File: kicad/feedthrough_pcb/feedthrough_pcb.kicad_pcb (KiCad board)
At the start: 2 copper layers, 150 x 150 mm, 2 parts, among them U1 LSHM-110-02.5-L-DV-A-S-TR, U2 LSHM-110-02.5-L-DV-A-S-TR

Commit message: updated feedthrough pcb
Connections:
- U2 pad 1: Net-(U1-Pad1) -> Net-(U2-Pad1)
- U2 pad 11: Net-(U1-Pad11) -> Net-(U2-Pad11)
- U2 pad 13: Net-(U1-Pad13) -> Net-(U2-Pad13)
- U2 pad 15: Net-(U1-Pad15) -> Net-(U2-Pad15)
- U2 pad 17: Net-(U1-Pad17) -> Net-(U2-Pad17)
- U2 pad 19: Net-(U1-Pad19) -> Net-(U2-Pad19)
- U2 pad 3: Net-(U1-Pad3) -> Net-(U2-Pad3)
- U2 pad 5: Net-(U1-Pad5) -> Net-(U2-Pad5)
- U2 pad 7: Net-(U1-Pad7) -> Net-(U2-Pad7)
- U2 pad 9: Net-(U1-Pad9) -> Net-(U2-Pad9)
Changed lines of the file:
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@@
     (zones 0)
     (modules 2)
-    (nets 21)
+    (nets 31)
   )
   (page A4)
@@
   )
   (setup
-    (last_trace_width 0.1524)
+    (last_trace_width 0.25)
     (user_trace_width 0.1524)
     (trace_clearance 0.2)
@@
     (solder_mask_min_width 0.25)
     (aux_axis_origin 0 0)
-    (visible_elements FFFFFF7F)
+    (visible_elements 7FFFFFFF)
     (pcbplotparams
       (layerselection 0x010fc_ffffffff)
@@
   (net 19 "Net-(U1-Pad19)")
   (net 20 "Net-(U1-Pad20)")
+  (net 21 "Net-(U2-Pad19)")
+  (net 22 "Net-(U2-Pad17)")
+  (net 23 "Net-(U2-Pad15)")
+  (net 24 "Net-(U2-Pad13)")
+  (net 25 "Net-(U2-Pad11)")
+  (net 26 "Net-(U2-Pad9)")
+  (net 27 "Net-(U2-Pad7)")
+  (net 28 "Net-(U2-Pad5)")
+  (net 29 "Net-(U2-Pad3)")
+  (net 30 "Net-(U2-Pad1)")
   (net_class Default "This is the default net class."
     (clearance 0.2)
@@
     (add_net "Net-(U1-Pad8)")
     (add_net "Net-(U1-Pad9)")
+    (add_net "Net-(U2-Pad1)")
+    (add_net "Net-(U2-Pad11)")
+    (add_net "Net-(U2-Pad13)")
+    (add_net "Net-(U2-Pad15)")
+    (add_net "Net-(U2-Pad17)")
+    (add_net "Net-(U2-Pad19)")
+    (add_net "Net-(U2-Pad3)")
+    (add_net "Net-(U2-Pad5)")
+    (add_net "Net-(U2-Pad7)")
+    (add_net "Net-(U2-Pad9)")
   )
   (module feedthrough_pcb:LSHM-110-02.5-L-DV-A-S-TR (layer B.Cu)
@@
       (effects (font (size 1 1) (thickness 0.15)) (justify mirror))
     )
-    (fp_text value LSHM-110-02.5-L-DV-A-S-TR (at 0 3.81) (layer B.Fab) hide
+    (fp_text value LSHM-110-02.5-L-DV-A-S-TR (at 0.1 -5.2) (layer B.Fab) hide
       (effects (font (size 1 1) (thickness 0.15)) (justify mirror))
     )
@@
       (effects (font (size 1 1) (thickness 0.15)))
     )
-    (fp_text value LSHM-110-02.5-L-DV-A-S-TR (at 0 -3.81) (layer F.Fab) hide
+    (fp_text value LSHM-110-02.5-L-DV-A-S-TR (at 0 5.5) (layer F.Fab) hide
       (effects (font (size 1 1) (thickness 0.15)))
     )
@@
       (net 20 "Net-(U1-Pad20)"))
     (pad 19 smd rect (at -2.29 1.75) (size 0.3 1.5) (layers F.Cu F.Paste F.Mask)
-      (net 19 "Net-(U1-Pad19)"))
+      (net 21 "Net-(U2-Pad19)"))
     (pad 18 smd rect (at -1.79 -1.75) (size 0.3 1.5) (layers F.Cu F.Paste F.Mask)
       (net 18 "Net-(U1-Pad18)"))
     (pad 17 smd rect (at -1.79 1.75) (size 0.3 1.5) (layers F.Cu F.Paste F.Mask)
-      (net 17 "Net-(U1-Pad17)"))
+      (net 22 "Net-(U2-Pad17)"))
     (pad 16 smd rect (at -1.29 -1.75) (size 0.3 1.5) (layers F.Cu F.Paste F.Mask)
       (net 16 "Net-(U1-Pad16)"))
     (pad 15 smd rect (at -1.29 1.75) (size 0.3 1.5) (layers F.Cu F.Paste F.Mask)
-      (net 15 "Net-(U1-Pad15)"))
+      (net 23 "Net-(U2-Pad15)"))
     (pad 14 smd rect (at -0.79 -1.75) (size 0.3 1.5) (layers F.Cu F.Paste F.Mask)
       (net 14 "Net-(U1-Pad14)"))
     (pad 13 smd rect (at -0.79 1.75) (size 0.3 1.5) (layers F.Cu F.Paste F.Mask)
-      (net 13 "Net-(U1-Pad13)"))
+      (net 24 "Net-(U2-Pad13)"))
     (pad 12 smd rect (at -0.29 -1.75) (size 0.3 1.5) (layers F.Cu F.Paste F.Mask)
       (net 12 "Net-(U1-Pad12)"))
     (pad 11 smd rect (at -0.29 1.75) (size 0.3 1.5) (layers F.Cu F.Paste F.Mask)
-      (net 11 "Net-(U1-Pad11)"))
+      (net 25 "Net-(U2-Pad11)"))
     (pad 10 smd rect (at 0.21 -1.75) (size 0.3 1.5) (layers F.Cu F.Paste F.Mask)
       (net 10 "Net-(U1-Pad10)"))
     (pad 9 smd rect (at 0.21 1.75) (size 0.3 1.5) (layers F.Cu F.Paste F.Mask)
-      (net 9 "Net-(U1-Pad9)"))
+      (net 26 "Net-(U2-Pad9)"))
     (pad 8 smd rect (at 0.71 -1.75) (size 0.3 1.5) (layers F.Cu F.Paste F.Mask)
       (net 8 "Net-(U1-Pad8)"))
     (pad 7 smd rect (at 0.71 1.75) (size 0.3 1.5) (layers F.Cu F.Paste F.Mask)
-      (net 7 "Net-(U1-Pad7)"))
+      (net 27 "Net-(U2-Pad7)"))
     (pad 6 smd rect (at 1.21 -1.75) (size 0.3 1.5) (layers F.Cu F.Paste F.Mask)
       (net 6 "Net-(U1-Pad6)"))
     (pad 5 smd rect (at 1.21 1.75) (size 0.3 1.5) (layers F.Cu F.Paste F.Mask)
-      (net 5 "Net-(U1-Pad5)"))
+      (net 28 "Net-(U2-Pad5)"))
     (pad 4 smd rect (at 1.71 -1.75) (size 0.3 1.5) (layers F.Cu F.Paste F.Mask)
       (net 4 "Net-(U1-Pad4)"))
     (pad 3 smd rect (at 1.71 1.75) (size 0.3 1.5) (layers F.Cu F.Paste F.Mask)
-      (net 3 "Net-(U1-Pad3)"))
+      (net 29 "Net-(U2-Pad3)"))
     (pad 2 smd rect (at 2.21 -1.75) (size 0.3 1.5) (layers F.Cu F.Paste F.Mask)
       (net 2 "Net-(U1-Pad2)"))
     (pad 1 smd rect (at 2.21 1.75) (size 0.3 1.5) (layers F.Cu F.Paste F.Mask)
-      (net 1 "Net-(U1-Pad1)"))
+      (net 30 "Net-(U2-Pad1)"))
   )
   (gr_circle (center 99.96 97.25) (end 174.96 97.25) (layer Edge.Cuts) (width 0.05))
-  (via (at 97.71 95) (size 0.5048) (drill 0.3) (layers F.Cu B.Cu) (net 20))
-  (via (at 98.21 99.5) (size 0.5048) (drill 0.3) (layers F.Cu B.Cu) (net 18))
-  (via (at 99.21 99.5) (size 0.5048) (drill 0.3) (layers F.Cu B.Cu) (net 14))
-  (via (at 100.21 99.5) (size 0.5048) (drill 0.3) (layers F.Cu B.Cu) (net 10))
-  (via (at 101.21 99.5) (size 0.5048) (drill 0.3) (layers F.Cu B.Cu) (net 6))
   (via (at 102.21 99.5) (size 0.5048) (drill 0.3) (layers F.Cu B.Cu) (net 2))
   (segment (start 102.21 98.25) (end 102.21 99.5) (width 0.1524) (layer F.Cu) (net 2))
@@
   (segment (start 101.71 97.51) (end 101.71 95) (width 0.1524) (layer F.Cu) (net 4))
   (segment (start 101.71 98.25) (end 101.71 97.51) (width 0.1524) (layer F.Cu) (net 4))
+  (via (at 101.21 99.5) (size 0.5048) (drill 0.3) (layers F.Cu B.Cu) (net 6))
   (segment (start 101.21 98.25) (end 101.21 99.5) (width 0.1524) (layer F.Cu) (net 6))
   (segment (start 101.21 96.99) (end 101.21 99.5) (width 0.1524) (layer B.Cu) (net 6))
@@
   (via (at 100.71 95) (size 0.5048) (drill 0.3) (layers F.Cu B.Cu) (net 8))
   (segment (start 100.71 98.25) (end 100.71 95) (width 0.1524) (layer F.Cu) (net 8))
+  (via (at 100.21 99.5) (size 0.5048) (drill 0.3) (layers F.Cu B.Cu) (net 10))
   (segment (start 100.21 98.25) (end 100.21 99.5) (width 0.1524) (layer F.Cu) (net 10))
   (segment (start 100.21 96.25) (end 100.21 99.5) (width 0.1524) (layer B.Cu) (net 10))
@@
   (via (at 99.71 95) (size 0.5048) (drill 0.3) (layers F.Cu B.Cu) (net 12))
   (segment (start 99.71 98.25) (end 99.71 95) (width 0.1524) (layer F.Cu) (net 12))
+  (via (at 99.21 99.5) (size 0.5048) (drill 0.3) (layers F.Cu B.Cu) (net 14))
   (segment (start 99.21 98.25) (end 99.21 99.5) (width 0.1524) (layer F.Cu) (net 14))
   (segment (start 99.21 96.25) (end 99.21 99.5) (width 0.1524) (layer B.Cu) (net 14))
@@
   (via (at 98.71 95) (size 0.5048) (drill 0.3) (layers F.Cu B.Cu) (net 16))
   (segment (start 98.71 98.25) (end 98.71 95) (width 0.1524) (layer F.Cu) (net 16))
+  (via (at 98.21 99.5) (size 0.5048) (drill 0.3) (layers F.Cu B.Cu) (net 18))
   (segment (start 98.21 98.25) (end 98.21 99.5) (width 0.1524) (layer F.Cu) (net 18))
   (segment (start 98.21 96.25) (end 98.21 99.5) (width 0.1524) (layer B.Cu) (net 18))
+  (via (at 97.71 95) (size 0.5048) (drill 0.3) (layers F.Cu B.Cu) (net 20))
   (segment (start 97.71 96.25) (end 97.71 95) (width 0.1524) (layer B.Cu) (net 20))
   (segment (start 97.71 97.3476) (end 97.71 95) (width 0.1524) (layer F.Cu) (net 20))

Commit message: updated feedthrough pcb
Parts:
- added U3: LSHM-110-02.5-L-DV-A-S-TR, feedthrough_pcb:LSHM-110-02.5-L-DV-A-S-TR, B.Cu at (87.7, 93.0)
- added U4: LSHM-110-02.5-L-DV-A-S-TR, feedthrough_pcb:LSHM-110-02.5-L-DV-A-S-TR, F.Cu at (87.7, 101.5)
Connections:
- U1 pad 1: Net-(U1-Pad1) -> GND
- U1 pad 11: Net-(U1-Pad11) -> GND
- U1 pad 13: Net-(U1-Pad13) -> GND
- U1 pad 15: Net-(U1-Pad15) -> GND
- U1 pad 17: Net-(U1-Pad17) -> GND
- U1 pad 19: Net-(U1-Pad19) -> GND
- U1 pad 3: Net-(U1-Pad3) -> GND
- U1 pad 41: (no net) -> GND
- U1 pad 5: Net-(U1-Pad5) -> GND
- U1 pad 7: Net-(U1-Pad7) -> GND
- U1 pad 9: Net-(U1-Pad9) -> GND
- U2 pad 1: Net-(U2-Pad1) -> GND
- U2 pad 11: Net-(U2-Pad11) -> GND
- U2 pad 13: Net-(U2-Pad13) -> GND
- U2 pad 15: Net-(U2-Pad15) -> GND
- U2 pad 17: Net-(U2-Pad17) -> GND
- U2 pad 19: Net-(U2-Pad19) -> GND
- U2 pad 3: Net-(U2-Pad3) -> GND
- U2 pad 41: (no net) -> GND
- U2 pad 5: Net-(U2-Pad5) -> GND
- U2 pad 7: Net-(U2-Pad7) -> GND
- U2 pad 9: Net-(U2-Pad9) -> GND
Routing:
- net Net-(U3-Pad2): track 0.00 -> 5.93 mm, vias 0 -> 1
- net Net-(U3-Pad20): track 0.00 -> 5.92 mm, vias 0 -> 1
- net Net-(U3-Pad4): track 0.00 -> 5.72 mm, vias 0 -> 1
- net Net-(U3-Pad18): track 0.00 -> 5.72 mm, vias 0 -> 1
- net Net-(U3-Pad6): track 0.00 -> 5.52 mm, vias 0 -> 1
- net Net-(U3-Pad16): track 0.00 -> 5.51 mm, vias 0 -> 1
- net Net-(U3-Pad8): track 0.00 -> 5.31 mm, vias 0 -> 1
- net Net-(U3-Pad14): track 0.00 -> 5.30 mm, vias 0 -> 1
- net Net-(U3-Pad10): track 0.00 -> 5.10 mm, vias 0 -> 1
- net Net-(U3-Pad12): track 0.00 -> 5.10 mm, vias 0 -> 1
- added copper zone on B.Cu, net GND
- added copper zone on F.Cu, net GND
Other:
- board size 150 x 150 mm -> 75 x 75 mm

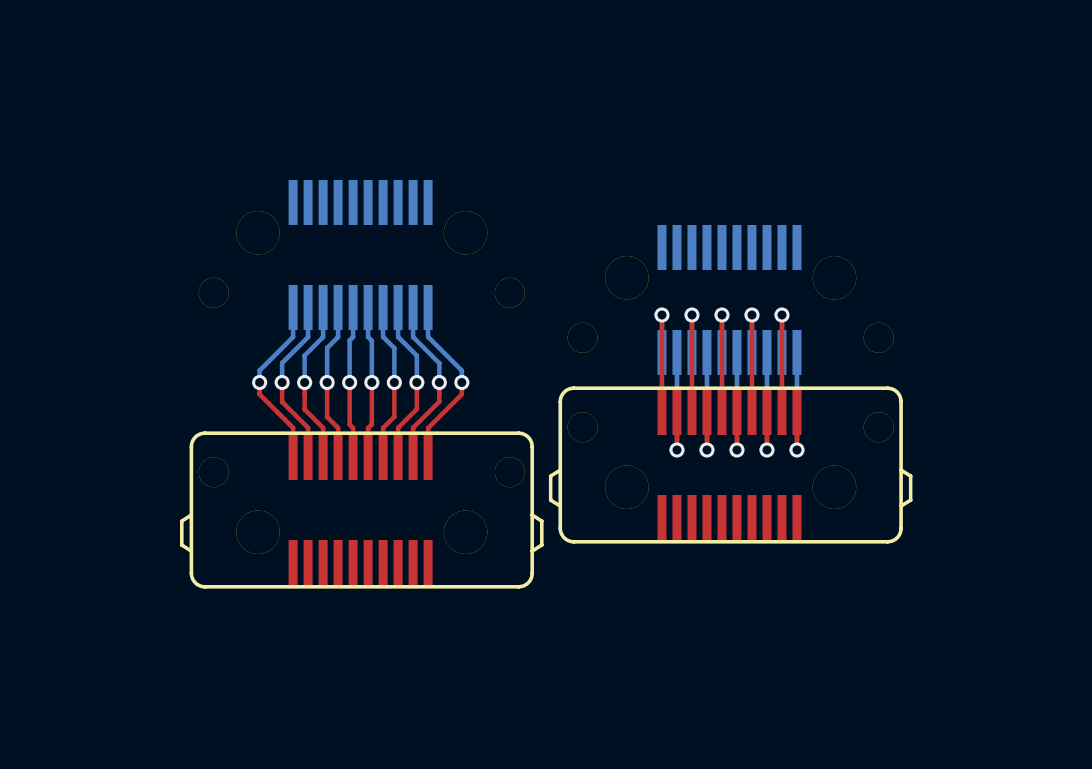
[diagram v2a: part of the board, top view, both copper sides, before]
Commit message: reorganised and added station04/05
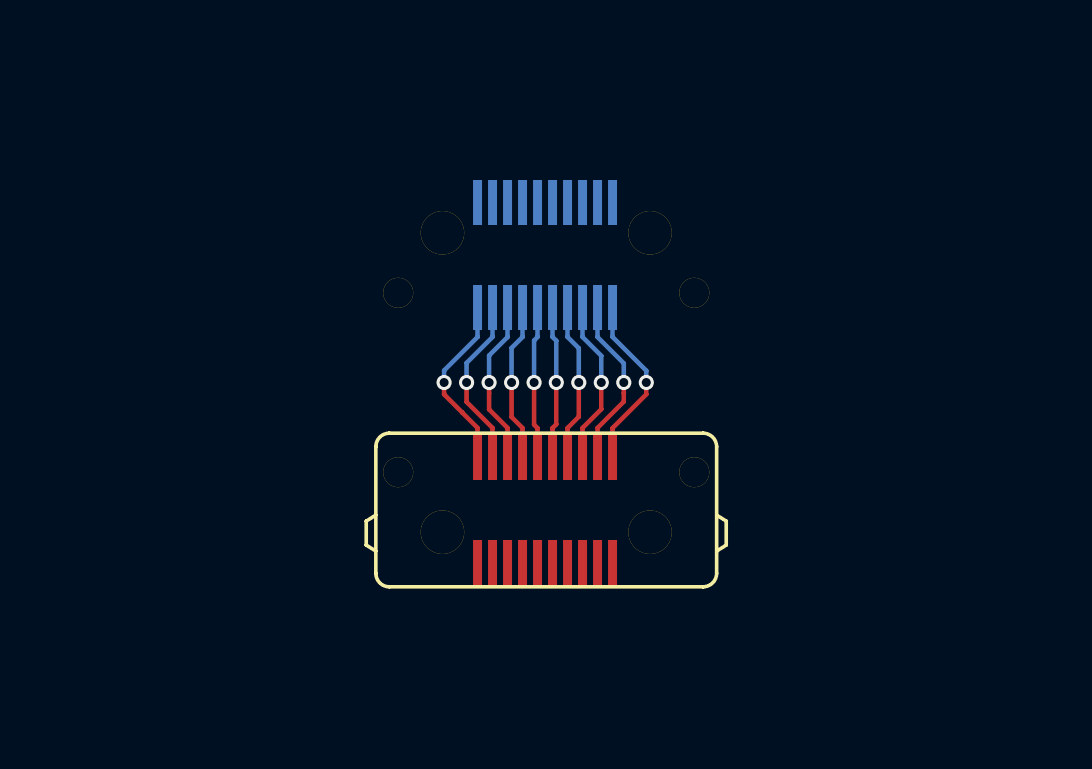
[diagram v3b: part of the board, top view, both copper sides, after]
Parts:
- removed U1, U2: LSHM-110-02.5-L-DV-A-S-TR, feedthrough_pcb:LSHM-110-02.5-L-DV-A-S-TR
- moved U3 6.15 mm to (93.9, 93.0)
- moved U4 6.15 mm to (93.9, 101.5)
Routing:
- net Net-(U1-Pad8): track 4.50 -> 0.00 mm, vias 1 -> 0
- net Net-(U1-Pad6): track 4.50 -> 0.00 mm, vias 1 -> 0
- net Net-(U1-Pad4): track 4.50 -> 0.00 mm, vias 1 -> 0
- net Net-(U1-Pad20): track 4.50 -> 0.00 mm, vias 1 -> 0
- net Net-(U1-Pad2): track 4.50 -> 0.00 mm, vias 1 -> 0
- net Net-(U1-Pad18): track 4.50 -> 0.00 mm, vias 1 -> 0
- net Net-(U1-Pad16): track 4.50 -> 0.00 mm, vias 1 -> 0
- net Net-(U1-Pad14): track 4.50 -> 0.00 mm, vias 1 -> 0
- net Net-(U1-Pad12): track 4.50 -> 0.00 mm, vias 1 -> 0
- net Net-(U1-Pad10): track 4.50 -> 0.00 mm, vias 1 -> 0

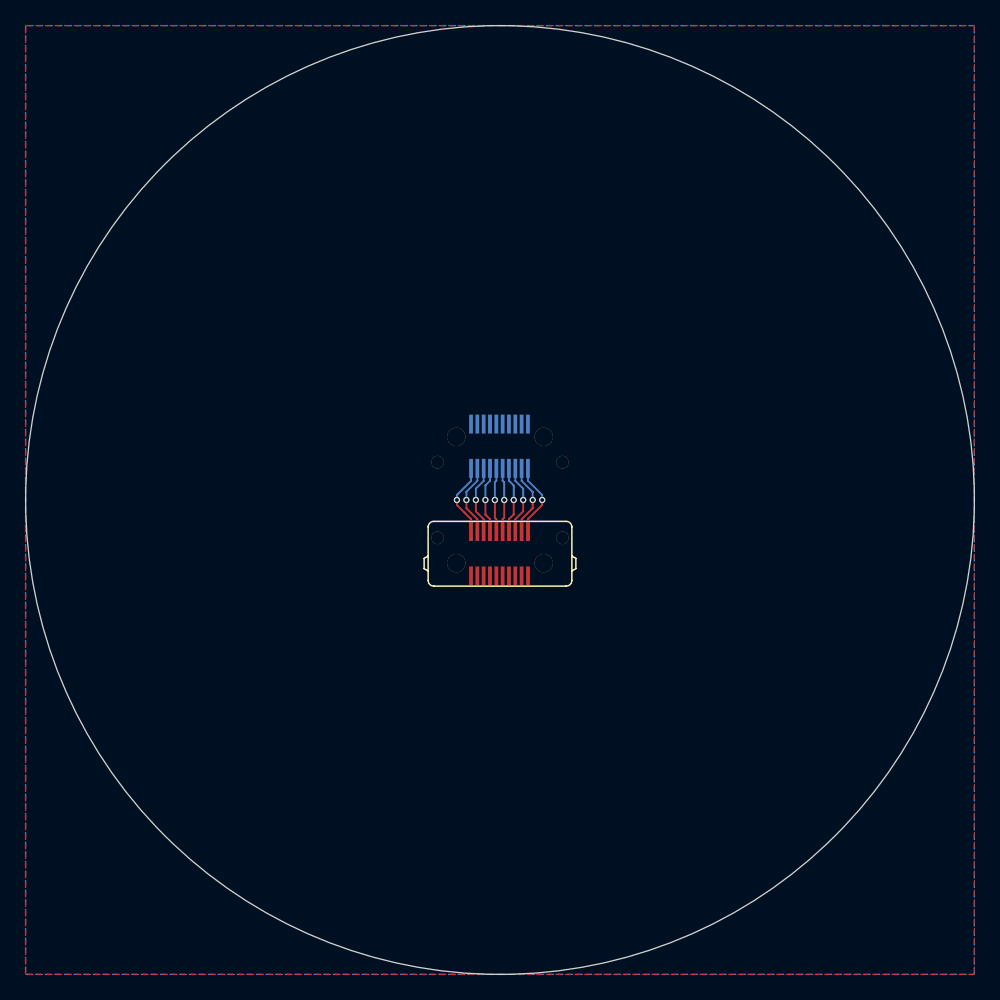
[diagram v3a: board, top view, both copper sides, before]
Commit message: added 3d models to feedthrough_pcb
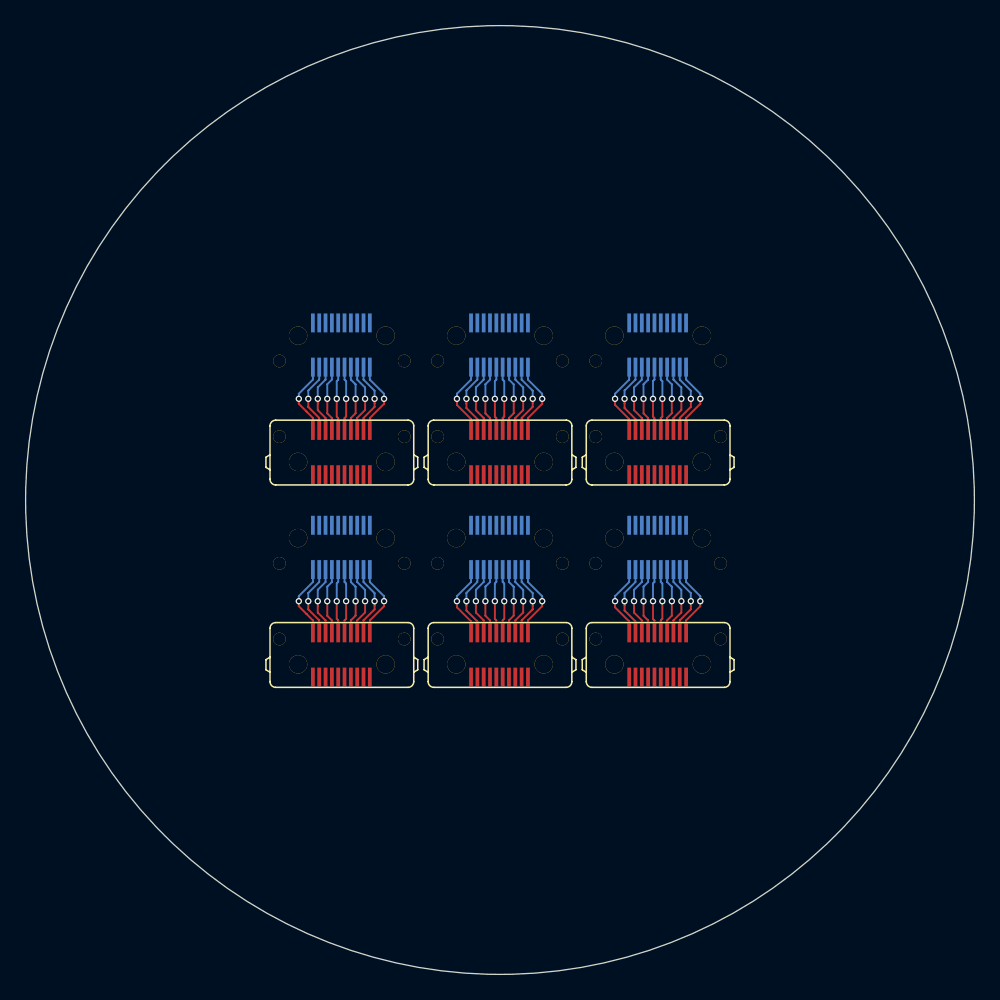
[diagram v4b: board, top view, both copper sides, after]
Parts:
- added U1: LSHM-110-02.5-L-DV-A-S-TR, feedthrough_pcb:LSHM-110-02.5-L-DV-A-S-TR, B.Cu at (81.4, 85.0)
- added U10: LSHM-110-02.5-L-DV-A-S-TR, feedthrough_pcb:LSHM-110-02.5-L-DV-A-S-TR, F.Cu at (93.9, 109.5)
- added U11: LSHM-110-02.5-L-DV-A-S-TR, feedthrough_pcb:LSHM-110-02.5-L-DV-A-S-TR, B.Cu at (106.4, 101.0)
- added U12: LSHM-110-02.5-L-DV-A-S-TR, feedthrough_pcb:LSHM-110-02.5-L-DV-A-S-TR, F.Cu at (106.4, 109.5)
- added U2: LSHM-110-02.5-L-DV-A-S-TR, feedthrough_pcb:LSHM-110-02.5-L-DV-A-S-TR, F.Cu at (81.4, 93.5)
- added U5: LSHM-110-02.5-L-DV-A-S-TR, feedthrough_pcb:LSHM-110-02.5-L-DV-A-S-TR, B.Cu at (106.4, 85.0)
- added U6: LSHM-110-02.5-L-DV-A-S-TR, feedthrough_pcb:LSHM-110-02.5-L-DV-A-S-TR, F.Cu at (106.4, 93.5)
- added U7: LSHM-110-02.5-L-DV-A-S-TR, feedthrough_pcb:LSHM-110-02.5-L-DV-A-S-TR, B.Cu at (81.4, 101.0)
- added U8: LSHM-110-02.5-L-DV-A-S-TR, feedthrough_pcb:LSHM-110-02.5-L-DV-A-S-TR, F.Cu at (81.4, 109.5)
- added U9: LSHM-110-02.5-L-DV-A-S-TR, feedthrough_pcb:LSHM-110-02.5-L-DV-A-S-TR, B.Cu at (93.9, 101.0)
- moved U3 8.00 mm to (93.9, 85.0)
- moved U4 8.00 mm to (93.9, 93.5)
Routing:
- net Net-(U7-Pad2): track 0.00 -> 5.93 mm, vias 0 -> 1
- net Net-(U5-Pad2): track 0.00 -> 5.93 mm, vias 0 -> 1
- net Net-(U11-Pad2): track 0.00 -> 5.93 mm, vias 0 -> 1
- net Net-(U10-Pad2): track 0.00 -> 5.93 mm, vias 0 -> 1
- net Net-(U1-Pad2): track 0.00 -> 5.93 mm, vias 0 -> 1
- net Net-(U5-Pad20): track 0.00 -> 5.92 mm, vias 0 -> 1
- net Net-(U11-Pad20): track 0.00 -> 5.92 mm, vias 0 -> 1
- net Net-(U10-Pad20): track 0.00 -> 5.92 mm, vias 0 -> 1
- net Net-(U7-Pad20): track 0.00 -> 5.92 mm, vias 0 -> 1
- net Net-(U1-Pad20): track 0.00 -> 5.92 mm, vias 0 -> 1
- net Net-(U7-Pad4): track 0.00 -> 5.72 mm, vias 0 -> 1
- net Net-(U5-Pad4): track 0.00 -> 5.72 mm, vias 0 -> 1
- net Net-(U11-Pad4): track 0.00 -> 5.72 mm, vias 0 -> 1
- net Net-(U10-Pad4): track 0.00 -> 5.72 mm, vias 0 -> 1
- net Net-(U1-Pad4): track 0.00 -> 5.72 mm, vias 0 -> 1
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- removed copper zone on B.Cu, net GND
- removed copper zone on F.Cu, net GND
